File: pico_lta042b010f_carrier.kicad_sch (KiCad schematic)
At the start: 23 parts, among them J1 LTA042B010F_FFC36, J2 5V INPUT, J3 13V8 OUT, U1 RaspberryPi_Pico_2W, U3 MC34063AD

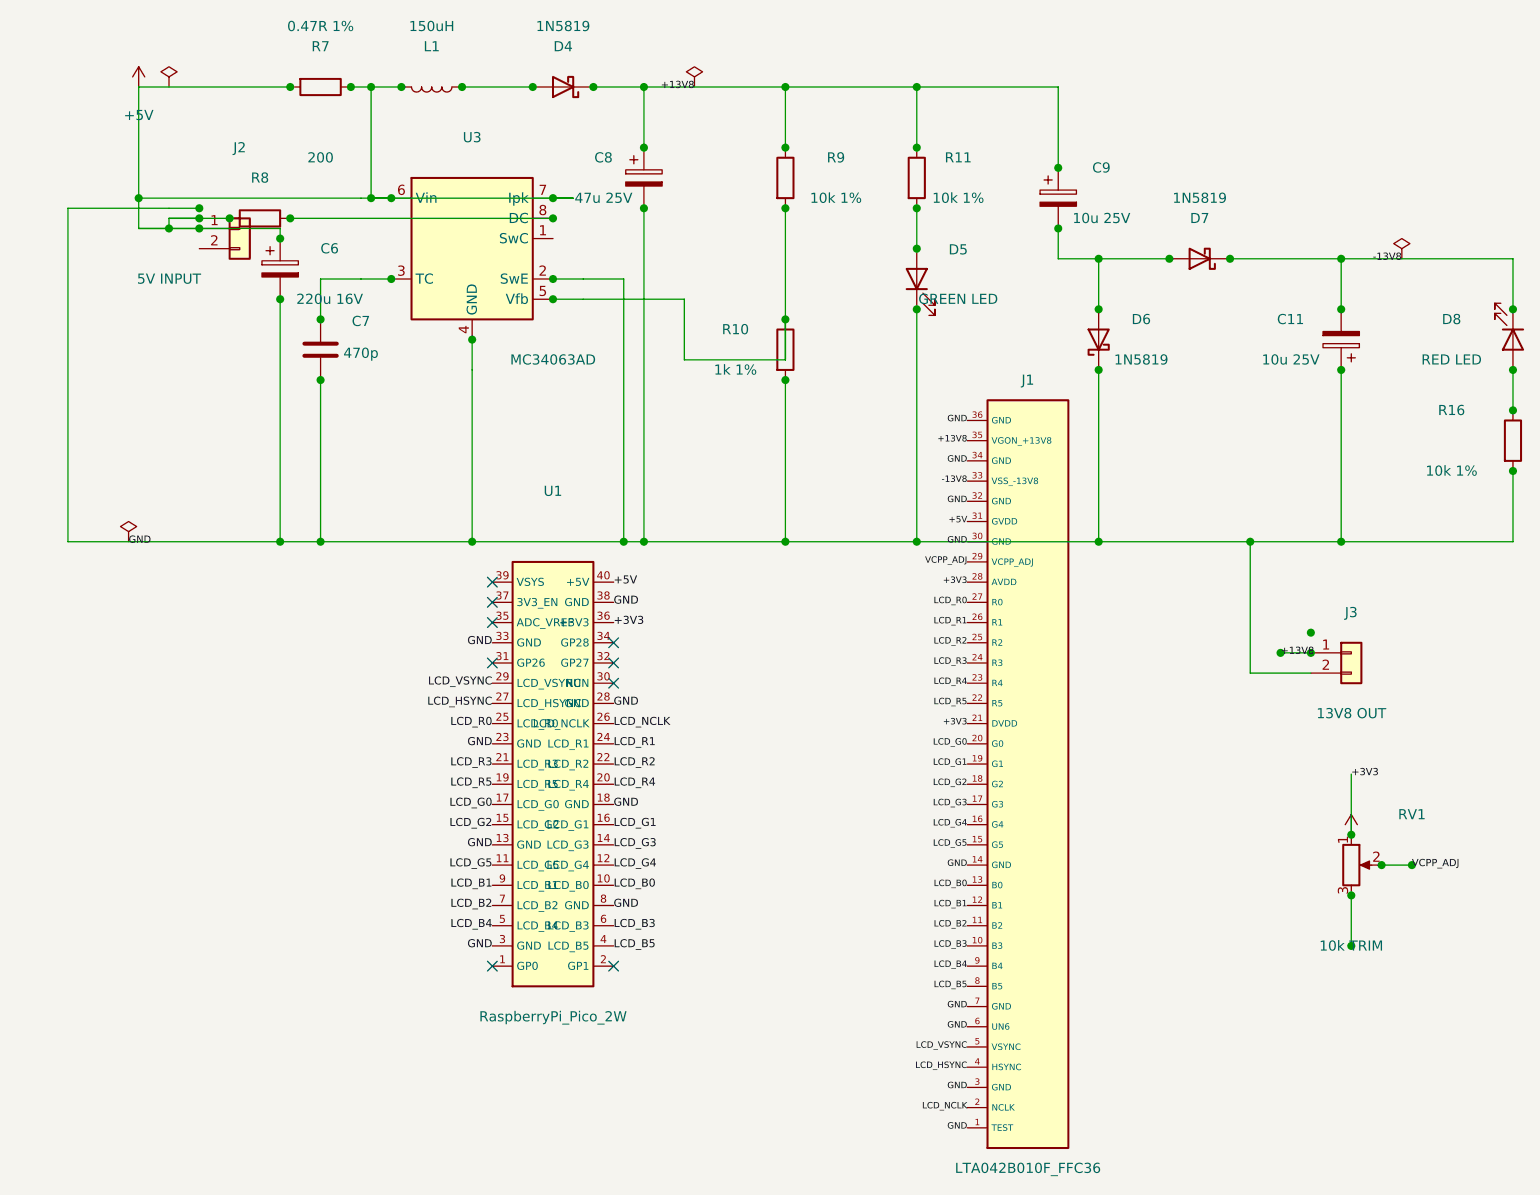
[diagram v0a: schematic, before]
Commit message: fix(kicad): clean power schematic routing
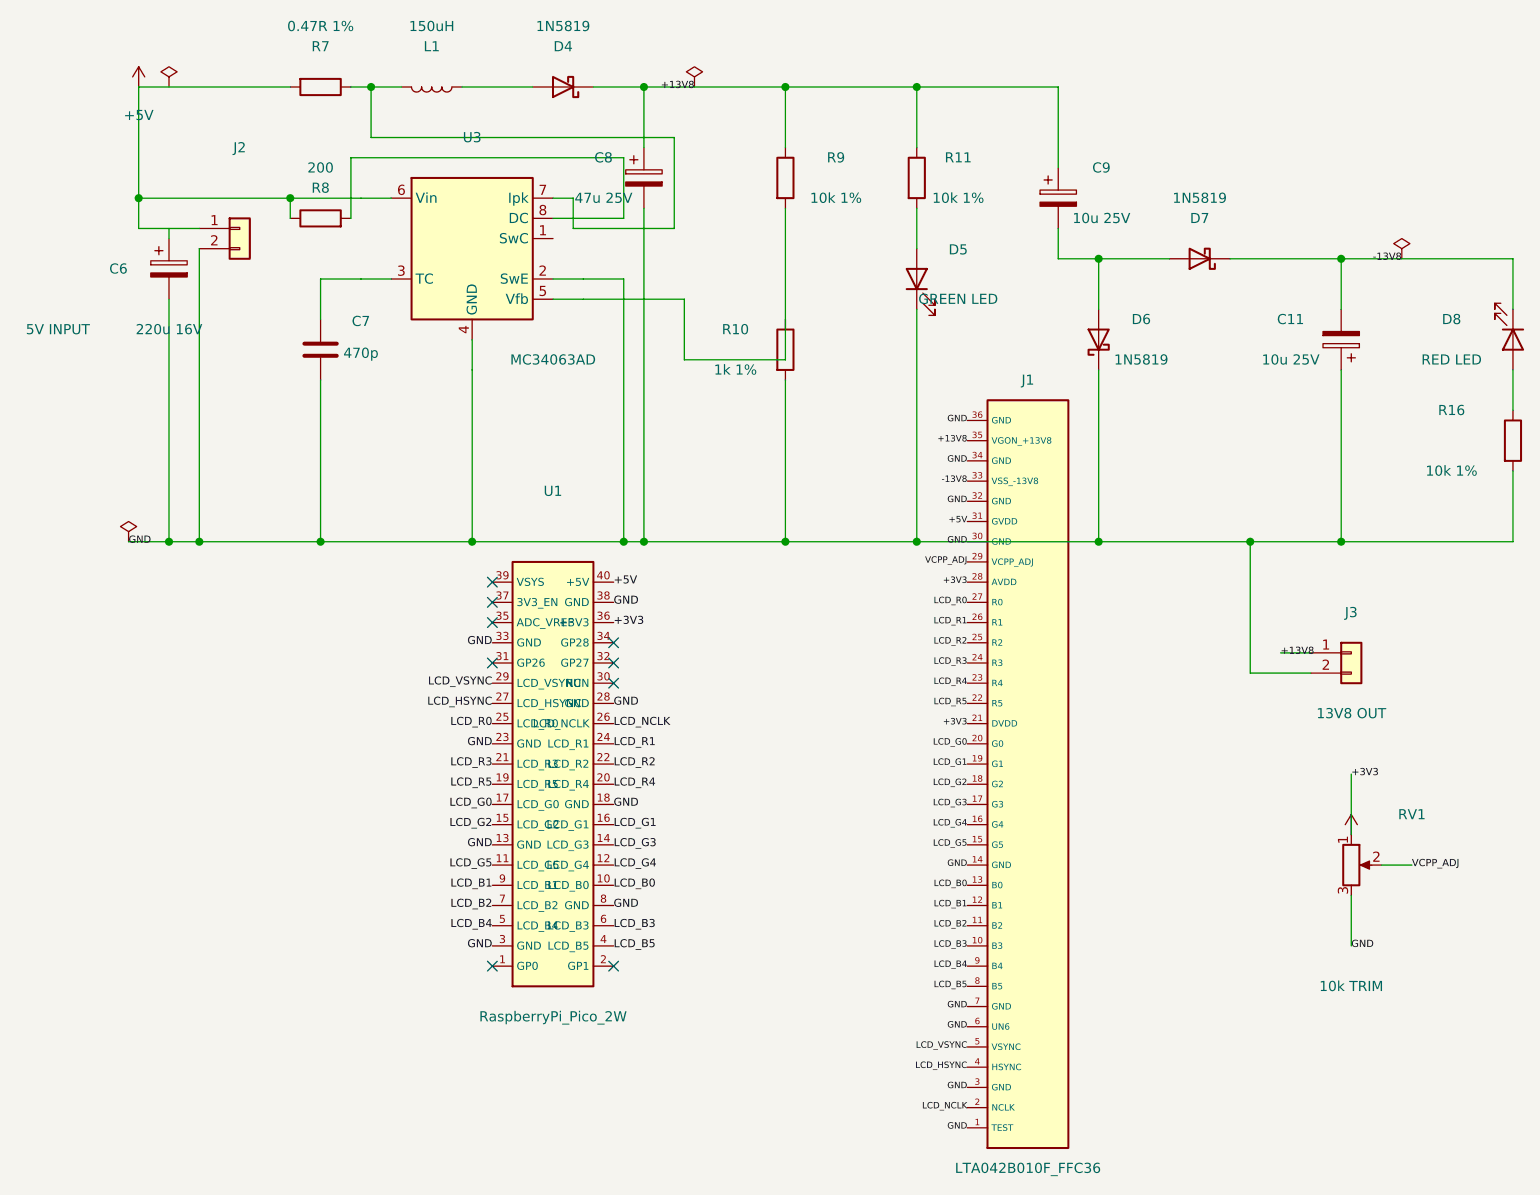
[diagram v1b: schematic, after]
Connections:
- net +5V: no longer L1.2, R7.1, U3.7 (Ipk)
- new net IPK_SENSE: L1.2, R7.1, U3.7 (Ipk)
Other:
- moved on the sheet: C6, R8
